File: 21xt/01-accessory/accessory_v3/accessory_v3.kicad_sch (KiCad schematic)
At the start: 23 parts, among them IC1 LT6658AHMSE-2.5#PBF, IC2 LT6658AHMSE-5#PBF, IC3 REF3450IDBVR

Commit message: Finished schematic and pcb rev 3
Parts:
- added L1: 15u, 21xt_footprints:IND_TCK-147_TRP, symbol Device:L
- added NT1: NetTie_2, NetTie:NetTie-2_SMD_Pad0.5mm, symbol Device:NetTie_2
- renumbered D2 to D11
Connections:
- net 12v_schot: now also L1.2; no longer PS1.2 (+VIN_(VCC))
- net GNDA: now also NT1.2; no longer C9.2, PS1.1 (-VIN_(GND))
- new net: L1.1, PS1.2 (+VIN_(VCC))
- new net B-: C9.2, NT1.1, PS1.1 (-VIN_(GND))
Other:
- note added: "L: 15 uH, .6 A f_c = 1 / (2pi sqrt(LC)) = 12,994 Hz"

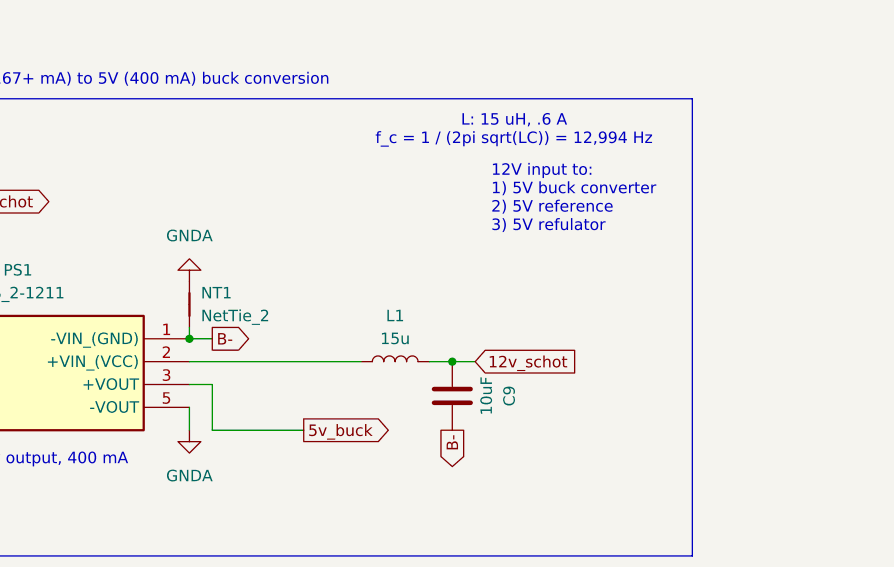
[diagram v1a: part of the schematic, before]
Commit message: Rerouting ethernet
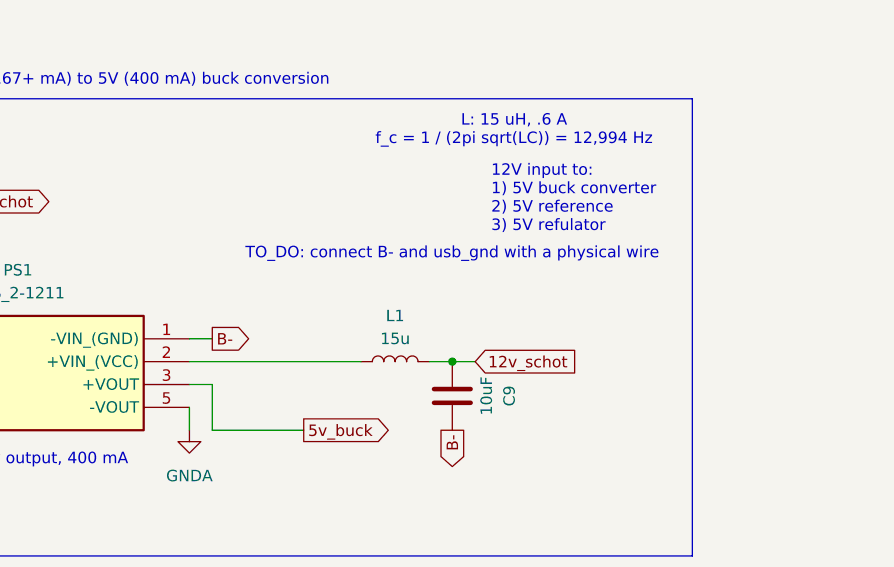
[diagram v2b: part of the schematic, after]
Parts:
- removed NT1: NetTie_2, NetTie:NetTie-2_SMD_Pad0.5mm, symbol Device:NetTie_2
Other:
- note added: "TO_DO: connect B- and usb_gnd with a physical wire"
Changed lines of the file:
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@@
-	)
-	(junction
-		(at 72.39 64.77)
-		(diameter 0)
-		(color 0 0 0 0)
 	)
 	(junction
@@
 	(wire
 		(pts
-			(xy 72.39 63.5) (xy 72.39 64.77)
-		)
-		(stroke
-			(width 0)
-			(type default)
-		)
-	)
-	(wire
-		(pts
 			(xy 226.06 120.65) (xy 226.06 121.92)
 		)
@@
 			)
 			(justify left bottom)
+		)
+	)
+	(text "TO_DO: connect B- and usb_gnd with a physical wire "
+		(exclude_from_sim no)
+		(at 101.6 55.372 0)
+		(effects
+			(font
+				(size 1.27 1.27)
+			)
 		)
 	)
@@
 	)
 	(symbol
-		(lib_id "Device:NetTie_2")
-		(at 72.39 60.96 90)
-		(unit 1)
-		(exclude_from_sim no)
-		(in_bom no)
-		(on_board yes)
-		(dnp no)
-		(fields_autoplaced yes)
-		(property "Reference" "NT1"
-			(at 73.66 59.6899 90)
-			(effects
-				(font
-					(size 1.27 1.27)
-				)
-				(justify right)
-			)
-		)
-		(property "Value" "NetTie_2"
-			(at 73.66 62.2299 90)
-			(effects
-				(font
-					(size 1.27 1.27)
-				)
-				(justify right)
-			)
-		)
-		(property "Footprint" "NetTie:NetTie-2_SMD_Pad0.5mm"
-			(at 72.39 60.96 0)
-			(effects
-				(font
-					(size 1.27 1.27)
-				)
-				(hide yes)
-			)
-		)
-		(property "Datasheet" "~"
-			(at 72.39 60.96 0)
-			(effects
-				(font
-					(size 1.27 1.27)
-				)
-				(hide yes)
-			)
-		)
-		(property "Description" "Net tie, 2 pins"
-			(at 72.39 60.96 0)
-			(effects
-				(font
-					(size 1.27 1.27)
-				)
-				(hide yes)
-			)
-		)
-		(pin "1"
-		)
-		(pin "2"
-		)
-		(instances
-			(project ""
-				(path "/5dacc41e-ffff-47d3-9300-200c6018c603"
-					(reference "NT1")
-					(unit 1)
-				)
-			)
-		)
-	)
-	(symbol
 		(lib_id "21xt_symbols:REF3450IDBVR")
 		(at 182.88 68.58 0)
@@
 					(unit 1)
 				)
-			)
-		)
-	)
-	(symbol
-		(lib_id "power:GNDA")
-		(at 72.39 58.42 180)
-		(unit 1)
-		(exclude_from_sim no)
-		(in_bom yes)
-		(on_board yes)
-		(dnp no)
-		(fields_autoplaced yes)
-		(property "Reference" "#PWR070"
-			(at 72.39 52.07 0)
-			(effects
-				(font
-					(size 1.27 1.27)
-				)
-				(hide yes)
-			)
-		)
-		(property "Value" "GNDA"
-			(at 72.39 53.34 0)
-			(effects
-				(font
-					(size 1.27 1.27)
-				)
-			)
-		)
-		(property "Footprint" ""
-			(at 72.39 58.42 0)
-			(effects
-				(font
-					(size 1.27 1.27)
-				)
-				(hide yes)
-			)
-		)
-		(property "Datasheet" ""
-			(at 72.39 58.42 0)
-			(effects
-				(font
-					(size 1.27 1.27)
-				)
-				(hide yes)
-			)
-		)
-		(property "Description" ""
-			(at 72.39 58.42 0)
-			(effects
-				(font
-					(size 1.27 1.27)
-				)
-				(hide yes)
-			)
-		)
-		(pin "1"
-		)
-		(instances
-			(project "accessory_v3"
-				(path "/5dacc41e-ffff-47d3-9300-200c6018c603"
-					(reference "#PWR070")
-					(unit 1)
-				)

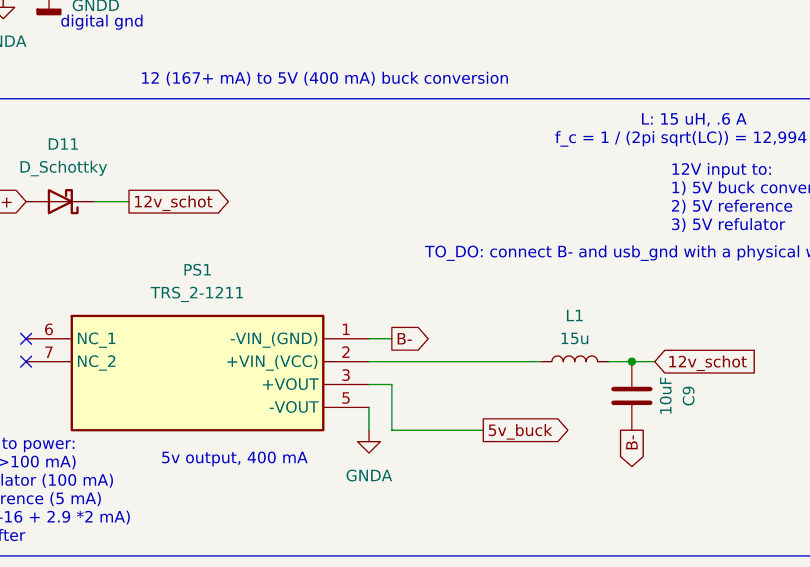
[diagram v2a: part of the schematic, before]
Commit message: Fixed edge cuts
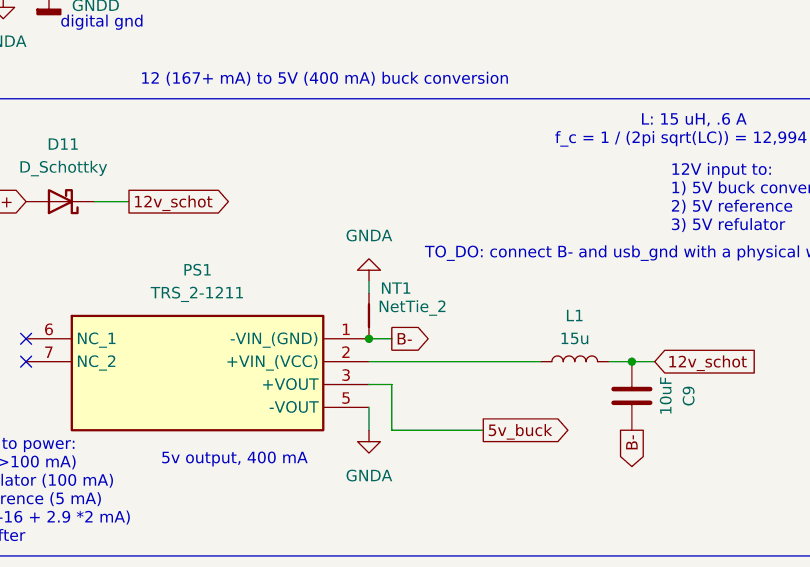
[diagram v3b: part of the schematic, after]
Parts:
- added NT1: NetTie_2, NetTie:NetTie-2_SMD_Pad0.5mm, symbol Device:NetTie_2
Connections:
- net B-: now also NT1.1
- net GNDA: now also NT1.2
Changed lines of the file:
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@@
 	(paper "A4")
+	(junction
+		(at 72.39 64.77)
+		(diameter 0)
+		(color 0 0 0 0)
+	)
 	(junction
 		(at 45.72 125.73)
@@
 		(pts
 			(xy 93.98 115.57) (xy 93.98 123.19)
+		)
+		(stroke
+			(width 0)
+			(type default)
+		)
+	)
+	(wire
+		(pts
+			(xy 72.39 58.42) (xy 72.39 59.69)
 		)
 		(stroke
@@
 	)
 	(symbol
+		(lib_id "Device:NetTie_2")
+		(at 72.39 62.23 90)
+		(unit 1)
+		(exclude_from_sim no)
+		(in_bom no)
+		(on_board yes)
+		(dnp no)
+		(property "Reference" "NT1"
+			(at 73.66 59.182 90)
+			(effects
+				(font
+					(size 1.27 1.27)
+				)
+				(justify right)
+			)
+		)
+		(property "Value" "NetTie_2"
+			(at 73.406 61.214 90)
+			(effects
+				(font
+					(size 1.27 1.27)
+				)
+				(justify right)
+			)
+		)
+		(property "Footprint" "NetTie:NetTie-2_SMD_Pad0.5mm"
+			(at 72.39 62.23 0)
+			(effects
+				(font
+					(size 1.27 1.27)
+				)
+				(hide yes)
+			)
+		)
+		(property "Datasheet" "~"
+			(at 72.39 62.23 0)
+			(effects
+				(font
+					(size 1.27 1.27)
+				)
+				(hide yes)
+			)
+		)
+		(property "Description" "Net tie, 2 pins"
+			(at 72.39 62.23 0)
+			(effects
+				(font
+					(size 1.27 1.27)
+				)
+				(hide yes)
+			)
+		)
+		(pin "1"
+		)
+		(pin "2"
+		)
+		(instances
+			(project ""
+				(path "/5dacc41e-ffff-47d3-9300-200c6018c603"
+					(reference "NT1")
+					(unit 1)
+				)
+			)
+		)
+	)
+	(symbol
 		(lib_id "Device:C")
 		(at 215.9 77.47 0)
@@
 					(unit 1)
 				)
+			)
+		)
+	)
+	(symbol
+		(lib_id "power:GNDA")
+		(at 72.39 58.42 0)
+		(mirror x)
+		(unit 1)
+		(exclude_from_sim no)
+		(in_bom yes)
+		(on_board yes)
+		(dnp no)
+		(property "Reference" "#PWR070"
+			(at 72.39 52.07 0)
+			(effects
+				(font
+					(size 1.27 1.27)
+				)
+				(hide yes)
+			)
+		)
+		(property "Value" "GNDA"
+			(at 72.39 53.34 0)
+			(effects
+				(font
+					(size 1.27 1.27)
+				)
+			)
+		)
+		(property "Footprint" ""
+			(at 72.39 58.42 0)
+			(effects
+				(font
+					(size 1.27 1.27)
+				)
+				(hide yes)
+			)
+		)
+		(property "Datasheet" ""
+			(at 72.39 58.42 0)
+			(effects
+				(font
+					(size 1.27 1.27)
+				)
+				(hide yes)
+			)
+		)
+		(property "Description" ""
+			(at 72.39 58.42 0)
+			(effects
+				(font
+					(size 1.27 1.27)
+				)
+				(hide yes)
+			)
+		)
+		(pin "1"
+		)
+		(instances
+			(project "accessory_v3"
+				(path "/5dacc41e-ffff-47d3-9300-200c6018c603"
+					(reference "#PWR070")
+					(unit 1)
+				)

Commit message: edited text
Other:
- note removed: "TO_DO: connect B- and usb_gnd with a physical wire"
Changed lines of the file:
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@@
-		)
-	)
-	(text "TO_DO: connect B- and usb_gnd with a physical wire "
-		(exclude_from_sim no)
-		(at 101.6 55.372 0)
-		(effects
-			(font
-				(size 1.27 1.27)
-			)
 		)
 	)
